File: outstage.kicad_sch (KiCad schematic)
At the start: 5 parts, among them J2001 Conn_01x06_Socket, J2002 Conn_01x06_Socket

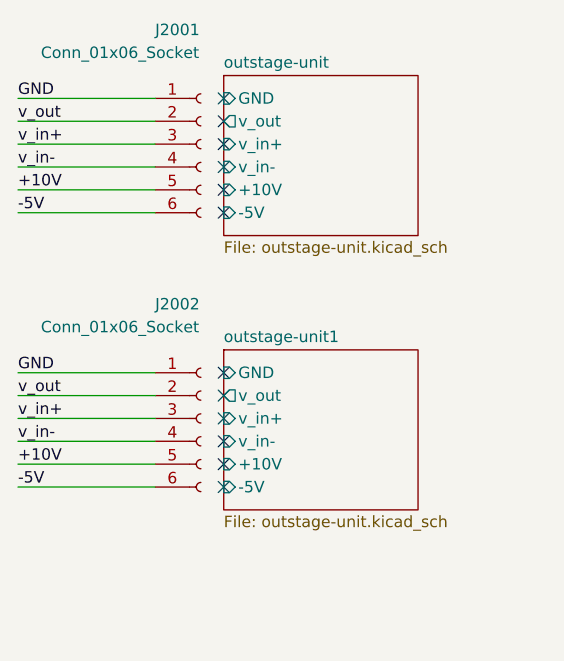
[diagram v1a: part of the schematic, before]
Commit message: edit outstage connector pin out for outstage-unit
enhance layout option with other pin out and mirror pinout for second outstage.
This allows to create a better layout with less crossing of high current tracks.
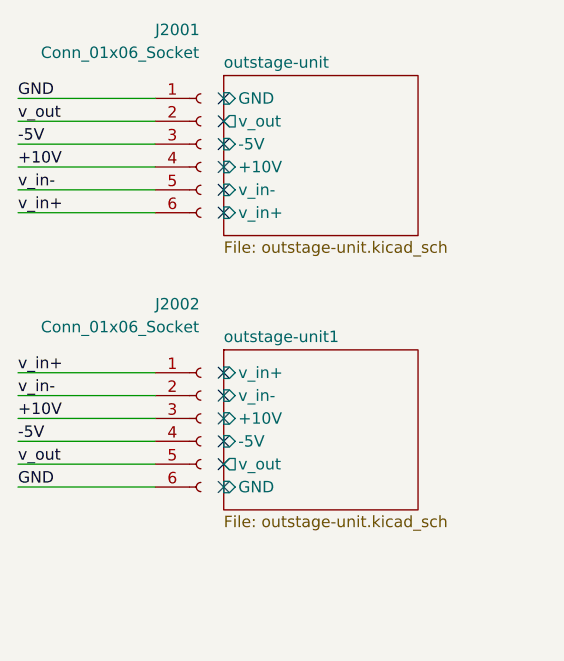
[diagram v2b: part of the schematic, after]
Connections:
- net +10V: now also J2001.4 (Pin_4), J2002.3 (Pin_3); no longer J2001.5 (Pin_5), J2002.5 (Pin_5)
- net -5V: now also J2001.3 (Pin_3), J2002.4 (Pin_4); no longer J2001.6 (Pin_6), J2002.6 (Pin_6)
- net GND: now also J2002.6 (Pin_6); no longer J2002.1 (Pin_1)
- net v_in+: now also J2001.6 (Pin_6), J2002.1 (Pin_1); no longer J2001.3 (Pin_3), J2002.3 (Pin_3)
- net v_in-: now also J2001.5 (Pin_5), J2002.2 (Pin_2); no longer J2001.4 (Pin_4), J2002.4 (Pin_4)
- net v_out: now also J2002.5 (Pin_5); no longer J2002.2 (Pin_2)
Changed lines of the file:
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@@
 	(title_block
 		(title "Power Supply Sink")
-		(date "2024-12-07")
-		(rev "0.13.4")
+		(date "2024-12-08")
+		(rev "0.13.5")
 		(company "Open Battery Tester")
 		(comment 1 "Outstage")
@@
 	)
 	(label "v_in-"
-		(at 125.73 85.09 0)
+		(at 125.73 87.63 0)
 		(fields_autoplaced yes)
 		(effects
@@
 	)
 	(label "GND"
-		(at 125.73 107.95 0)
+		(at 125.73 120.65 0)
 		(fields_autoplaced yes)
 		(effects
@@
 	)
 	(label "v_out"
-		(at 125.73 110.49 0)
+		(at 125.73 118.11 0)
 		(fields_autoplaced yes)
 		(effects
@@
 	)
 	(label "+10V"
-		(at 125.73 87.63 0)
+		(at 125.73 85.09 0)
 		(fields_autoplaced yes)
 		(effects
@@
 	)
 	(label "+10V"
-		(at 125.73 118.11 0)
+		(at 125.73 113.03 0)
 		(fields_autoplaced yes)
 		(effects
@@
 	)
 	(label "v_in-"
+		(at 125.73 110.49 0)
+		(fields_autoplaced yes)
+		(effects
+			(font
+				(size 1.27 1.27)
+			)
+			(justify left bottom)
+		)
+	)
+	(label "v_in+"
+		(at 125.73 90.17 0)
+		(fields_autoplaced yes)
+		(effects
+			(font
+				(size 1.27 1.27)
+			)
+			(justify left bottom)
+		)
+	)
+	(label "v_in+"
+		(at 125.73 107.95 0)
+		(fields_autoplaced yes)
+		(effects
+			(font
+				(size 1.27 1.27)
+			)
+			(justify left bottom)
+		)
+	)
+	(label "-5V"
+		(at 125.73 82.55 0)
+		(fields_autoplaced yes)
+		(effects
+			(font
+				(size 1.27 1.27)
+			)
+			(justify left bottom)
+		)
+	)
+	(label "-5V"
 		(at 125.73 115.57 0)
-		(fields_autoplaced yes)
-		(effects
-			(font
-				(size 1.27 1.27)
-			)
-			(justify left bottom)
-		)
-	)
-	(label "v_in+"
-		(at 125.73 82.55 0)
-		(fields_autoplaced yes)
-		(effects
-			(font
-				(size 1.27 1.27)
-			)
-			(justify left bottom)
-		)
-	)
-	(label "v_in+"
-		(at 125.73 113.03 0)
-		(fields_autoplaced yes)
-		(effects
-			(font
-				(size 1.27 1.27)
-			)
-			(justify left bottom)
-		)
-	)
-	(label "-5V"
-		(at 125.73 90.17 0)
-		(fields_autoplaced yes)
-		(effects
-			(font
-				(size 1.27 1.27)
-			)
-			(justify left bottom)
-		)
-	)
-	(label "-5V"
-		(at 125.73 120.65 0)
 		(fields_autoplaced yes)
 		(effects
@@
 		)
 		(pin "-5V" input
-			(at 148.59 90.17 180)
+			(at 148.59 82.55 180)
 			(effects
 				(font
@@
 		)
 		(pin "v_in-" input
+			(at 148.59 87.63 180)
+			(effects
+				(font
+					(size 1.27 1.27)
+				)
+				(justify left)
+			)
+		)
+		(pin "v_in+" input
+			(at 148.59 90.17 180)
+			(effects
+				(font
+					(size 1.27 1.27)
+				)
+				(justify left)
+			)
+		)
+		(pin "+10V" input
 			(at 148.59 85.09 180)
-			(effects
-				(font
-					(size 1.27 1.27)
-				)
-				(justify left)
-			)
-		)
-		(pin "v_in+" input
-			(at 148.59 82.55 180)
-			(effects
-				(font
-					(size 1.27 1.27)
-				)
-				(justify left)
-			)
-		)
-		(pin "+10V" input
-			(at 148.59 87.63 180)
 			(effects
 				(font
@@
 		)
 		(pin "GND" input
+			(at 148.59 120.65 180)
+			(effects
+				(font
+					(size 1.27 1.27)
+				)
+				(justify left)
+			)
+		)
+		(pin "-5V" input
+			(at 148.59 115.57 180)
+			(effects
+				(font
+					(size 1.27 1.27)
+				)
+				(justify left)
+			)
+		)
+		(pin "v_out" output
+			(at 148.59 118.11 180)
+			(effects
+				(font
+					(size 1.27 1.27)
+				)
+				(justify left)
+			)
+		)
+		(pin "v_in-" input
+			(at 148.59 110.49 180)
+			(effects
+				(font
+					(size 1.27 1.27)
+				)
+				(justify left)
+			)
+		)
+		(pin "v_in+" input
 			(at 148.59 107.95 180)
 			(effects
@@
 			)
 		)
-		(pin "-5V" input
-			(at 148.59 120.65 180)
-			(effects
-				(font
-					(size 1.27 1.27)
-				)
-				(justify left)
-			)
-		)
-		(pin "v_out" output
-			(at 148.59 110.49 180)
-			(effects
-				(font
-					(size 1.27 1.27)
-				)
-				(justify left)
-			)
-		)
-		(pin "v_in-" input
-			(at 148.59 115.57 180)
-			(effects
-				(font
-					(size 1.27 1.27)
-				)
-				(justify left)
-			)
-		)
-		(pin "v_in+" input
+		(pin "+10V" input
 			(at 148.59 113.03 180)
 			(effects
 				(font
-					(size 1.27 1.27)
-				)
-				(justify left)
-			)
-		)
-		(pin "+10V" input
-			(at 148.59 118.11 180)
-			(effects
-				(font
